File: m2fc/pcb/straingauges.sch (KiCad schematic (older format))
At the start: 81 parts, among them IC201 AD8226, IC202 AD8656, IC203 AD8541, IC204 AD8226, IC205 AD8656, IC206 AD8541, IC207 AD8226, IC208 AD8656, IC209 AD8541, K201 CONN_3, K202 CONN_3, K203 CONN_3, U201 HOUSING, U202 HOUSING, U203 HOUSING

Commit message: sd pullups, shielded sgs
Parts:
- removed K201, K202, K203: CONN_3, symbol CONN_3
- added P201, P202, P203: CONN_4, m2fc:S04B-PASK-2, symbol CONN_4
- C202: renamed from C209; footprint 0603 -> m2fc:C0603
- C204: renamed from C222; footprint 0603 -> m2fc:C0603
- C206: renamed from C235; footprint 0603 -> m2fc:C0603
- C208: renamed from C210; footprint 0603 -> m2fc:C0603
- C210: renamed from C223; footprint 0603 -> m2fc:C0603
- C212: renamed from C236; footprint 0603 -> m2fc:C0603
- C214: renamed from C211; footprint 0603 -> m2fc:C0603
- C216: renamed from C224; footprint 0603 -> m2fc:C0603
- C218: renamed from C237; footprint 0603 -> m2fc:C0603
- C219: renamed from C201; footprint 0603 -> m2fc:C0603
- C220: renamed from C214; footprint 0603 -> m2fc:C0603
- C221: renamed from C227; footprint 0603 -> m2fc:C0603
- C222: renamed from C207; footprint 0603 -> m2fc:C0603
- C223: renamed from C220; footprint 0603 -> m2fc:C0603
- C224: renamed from C233; footprint 0603 -> m2fc:C0603
- C225: renamed from C202; footprint 0603 -> m2fc:C0603
- C226: renamed from C215; footprint 0603 -> m2fc:C0603
- C227: renamed from C228; footprint 0603 -> m2fc:C0603
- C228: renamed from C212; footprint 0603 -> m2fc:C0603
- C229: renamed from C225; footprint 0603 -> m2fc:C0603
- C230: renamed from C238; footprint 0603 -> m2fc:C0603
- C234: renamed from C208; footprint 0603 -> m2fc:C0603
- C235: renamed from C221; footprint 0603 -> m2fc:C0603
- C236: renamed from C234; footprint 0603 -> m2fc:C0603
- C237: renamed from C203; footprint 0603 -> m2fc:C0603
- C238: renamed from C216; footprint 0603 -> m2fc:C0603
- C239: renamed from C229; footprint 0603 -> m2fc:C0603
- IC204: renamed from IC201; footprint SOIC8 -> m2fc:MSOP8
- IC205: renamed from IC204; footprint SOIC8 -> m2fc:MSOP8
- IC206: renamed from IC207; footprint SOIC8 -> m2fc:MSOP8
- IC207, IC208: renamed from IC202; footprint SOIC8 -> m2fc:SOIC8
- IC207, IC209: renamed from IC205; footprint SOIC8 -> m2fc:SOIC8
- IC208: footprint SOIC8 -> m2fc:SOIC8
- IC209: renamed from IC208; footprint SOIC8 -> m2fc:SOIC8
- R201, R211: footprint 0603 -> m2fc:R0603
- R202: renamed from R209; footprint 0603 -> m2fc:R0603
- R203: renamed from R217; footprint 0603 -> m2fc:R0603
- R204: renamed from R202; footprint 0603 -> m2fc:R0603
- R205: renamed from R208; footprint 0603 -> m2fc:R0603
- R206: renamed from R210; footprint 0603 -> m2fc:R0603
- R207: renamed from R216; footprint 0603 -> m2fc:R0603
- R208: renamed from R218; footprint 0603 -> m2fc:R0603
- R209: renamed from R224; footprint 0603 -> m2fc:R0603
- R210: renamed from R203; footprint 0603 -> m2fc:R0603
- R212: renamed from R219; footprint 0603 -> m2fc:R0603
- R213: renamed from R204; footprint 0603 -> m2fc:R0603
- R214: renamed from R212; footprint 0603 -> m2fc:R0603
- R215: renamed from R220; footprint 0603 -> m2fc:R0603
- R216: renamed from R205; footprint 0603 -> m2fc:R0603
- R217: renamed from R213; footprint 0603 -> m2fc:R0603
- R218: renamed from R221; footprint 0603 -> m2fc:R0603
- R219: renamed from R206; footprint 0603 -> m2fc:R0603
- R220: renamed from R214; footprint 0603 -> m2fc:R0603
- R221: renamed from R222; footprint 0603 -> m2fc:R0603
- R222: renamed from R207; footprint 0603 -> m2fc:R0603
- R223: renamed from R215; footprint 0603 -> m2fc:R0603
- R224: renamed from R223; footprint 0603 -> m2fc:R0603
- TP201, TP202, TP203: footprint (none) -> m2fc:TESTPAD
- U201, U202, U203: Farnell 1830728 -> 1830729
- renumbered C204 to C201, C217 to C203, C230 to C205, C205 to C207, C218 to C209, C231 to C211, C206 to C213, C219 to C215, C232 to C217, C213 to C231, C226 to C232, C239 to C233, IC203 to IC201, IC206 to IC202, IC209 to IC203
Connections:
- wire segments 225 -> 228

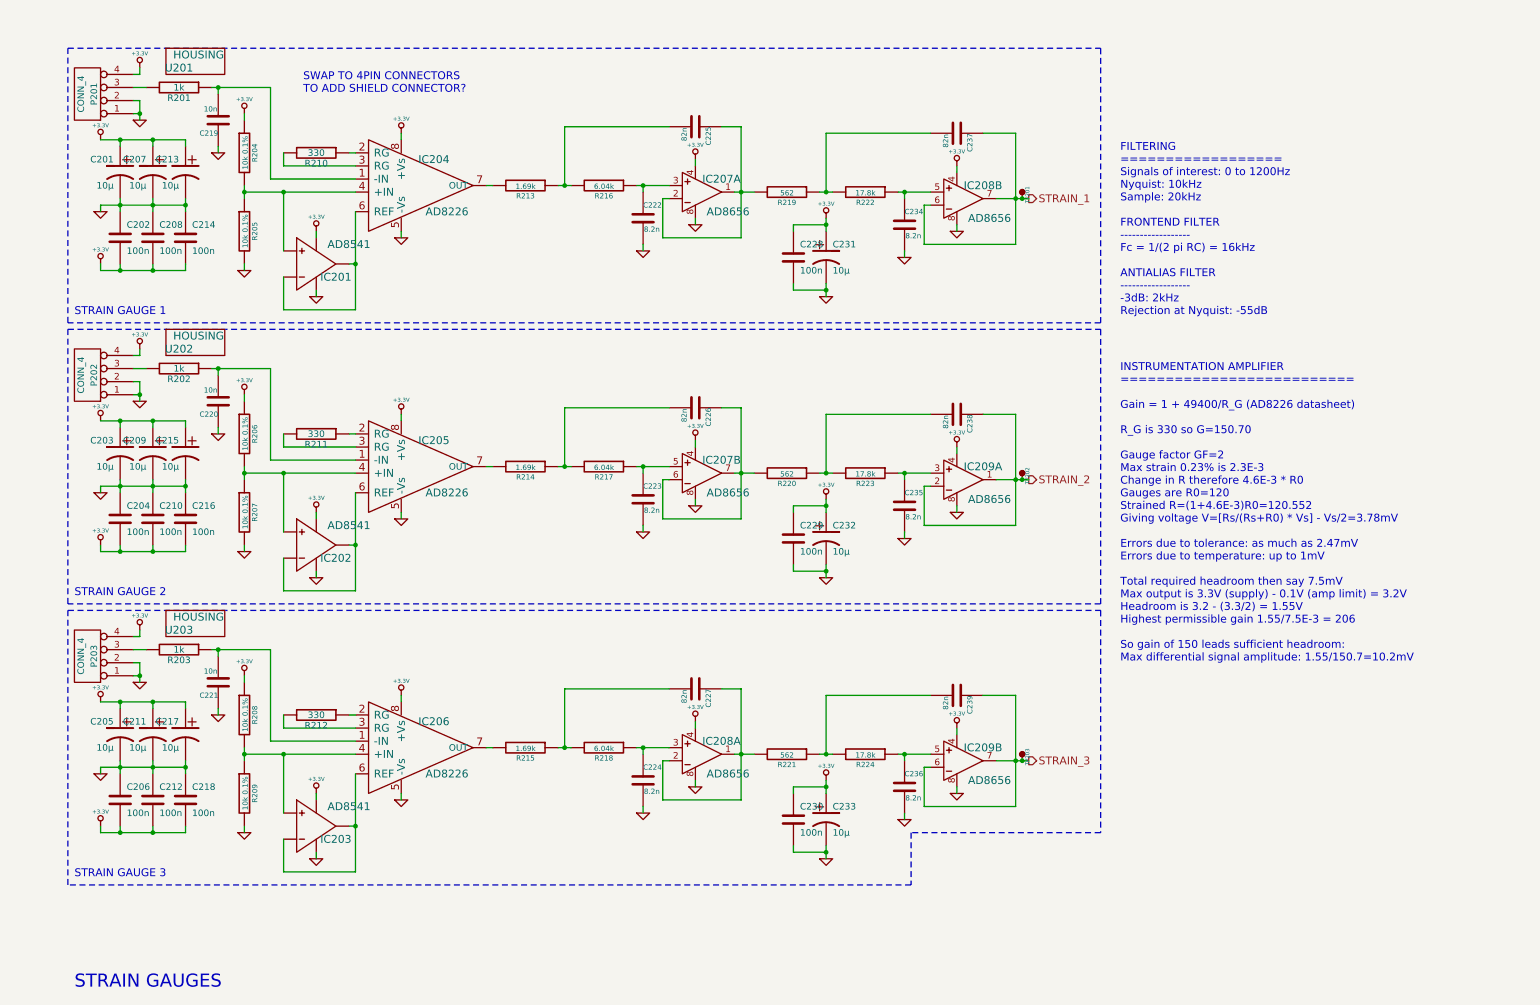
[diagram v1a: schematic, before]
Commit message: add esd diodes to m2fc
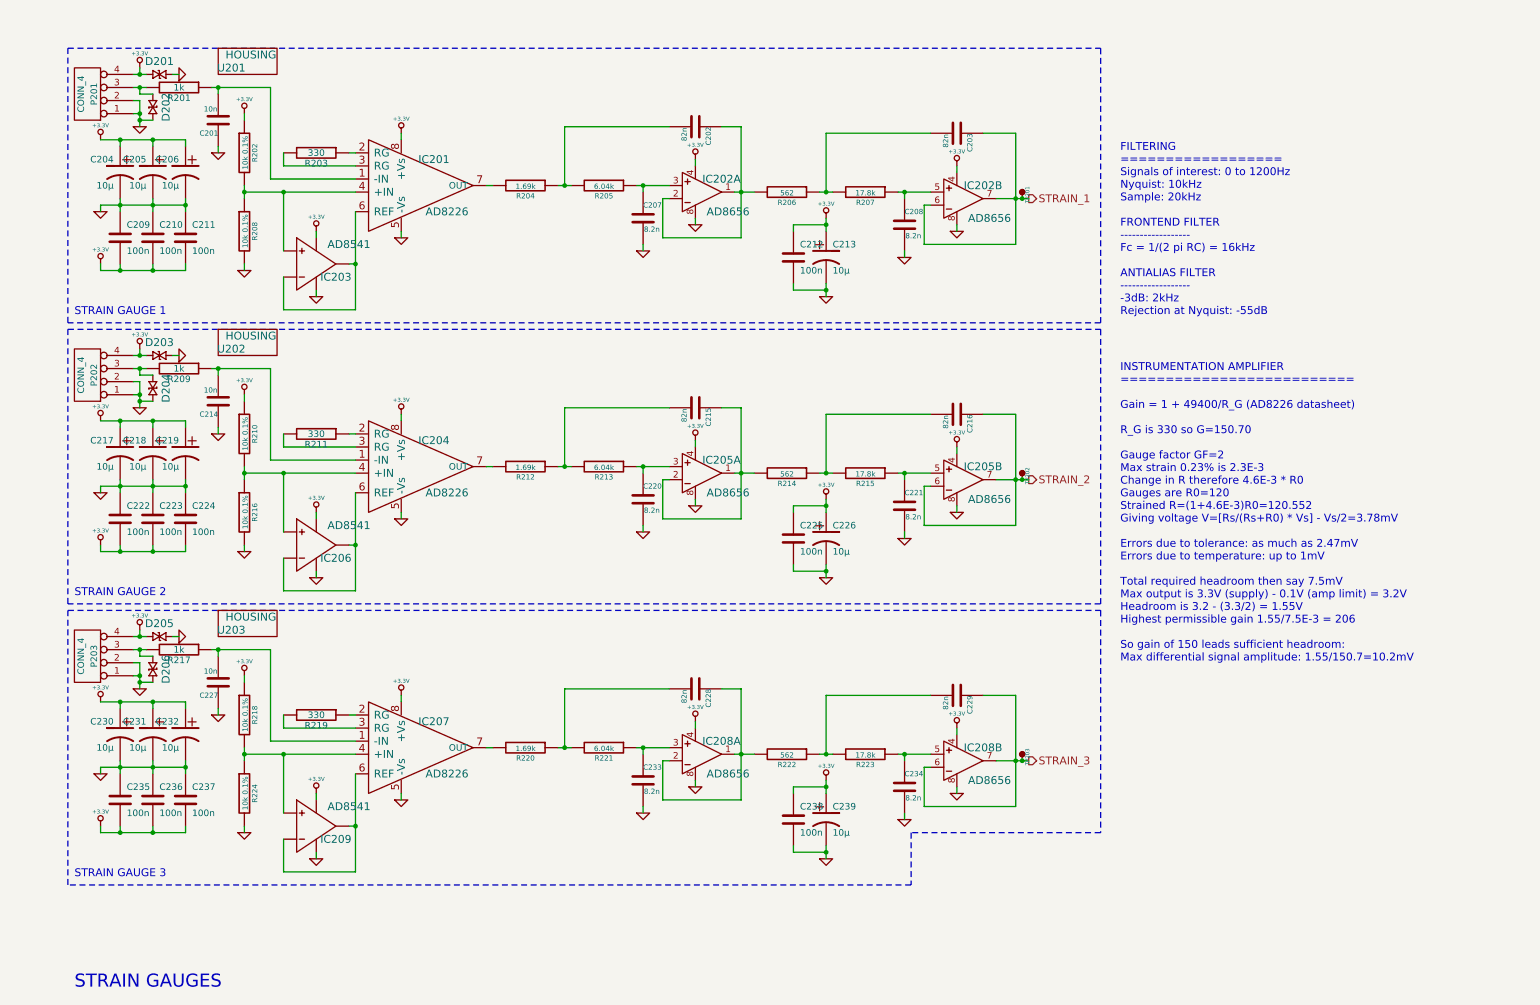
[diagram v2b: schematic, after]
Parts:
- added D201, D202, D203, D204, D205, D206: CGA0402MLC-12G, m2fc:R0402, symbol CGA0402MLC-12G
- C204: renamed from C201; footprint 1411 -> m2fc:C0603; Farnell 2333026 -> 1657936
- C205: renamed from C207; footprint 1411 -> m2fc:C0603; Farnell 2333026 -> 1657936
- C206: renamed from C213; footprint 1411 -> m2fc:C0603; Farnell 2333026 -> 1657936
- C213: renamed from C231; footprint 1411 -> m2fc:C0603; Farnell 2333026 -> 1657936
- C217: renamed from C203; footprint 1411 -> m2fc:C0603; Farnell 2333026 -> 1657936
- C218: renamed from C209; footprint 1411 -> m2fc:C0603; Farnell 2333026 -> 1657936
- C219: renamed from C215; footprint 1411 -> m2fc:C0603; Farnell 2333026 -> 1657936
- C226: renamed from C232; footprint 1411 -> m2fc:C0603; Farnell 2333026 -> 1657936
- C230: renamed from C205; footprint 1411 -> m2fc:C0603; Farnell 2333026 -> 1657936
- C231: renamed from C211; footprint 1411 -> m2fc:C0603; Farnell 2333026 -> 1657936
- C232: renamed from C217; footprint 1411 -> m2fc:C0603; Farnell 2333026 -> 1657936
- C239: renamed from C233; footprint 1411 -> m2fc:C0603; Farnell 2333026 -> 1657936
- renumbered C219 to C201, C225 to C202, C237 to C203, C222 to C207, C234 to C208, C202 to C209, C208 to C210, C214 to C211, C228 to C212, C220 to C214, C226 to C215, C238 to C216, C223 to C220, C235 to C221, C204 to C222, C210 to C223, C216 to C224, C229 to C225, C221 to C227, C227 to C228, C239 to C229, C224 to C233, C236 to C234, C206 to C235, C212 to C236, C218 to C237, C230 to C238, IC204 to IC201, IC207 to IC202, IC208 to IC202, IC201 to IC203, IC205 to IC204, IC207 to IC205, IC209 to IC205, IC202 to IC206, IC206 to IC207, IC209 to IC208, IC203 to IC209, R204 to R202, R210 to R203, R213 to R204, R216 to R205, R219 to R206, R222 to R207, R205 to R208, R202 to R209, R206 to R210, R214 to R212, R217 to R213, R220 to R214, R223 to R215, R207 to R216, R203 to R217, R208 to R218, R212 to R219, R215 to R220, R218 to R221, R221 to R222, R224 to R223, R209 to R224
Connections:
- net +3.3V: now also D201.2, D203.2, D205.2
- net GND: now also D201.1, D202.1, D203.1, D204.1, D205.1, D206.1
- net STRAIN_2: now also IC205.6 (-IN), IC205.7 (OUT); no longer IC205.1 (OUT), IC205.2 (-IN)
- net at P201.3 (P3), R201.2: now also D202.2
- net at P202.3 (P3), R209.2: now also D204.2
- net at C220.1, R213.1: now also IC205.3 (+IN); no longer IC205.5 (+IN)
- net at C215.1, R214.2: now also IC205.1 (OUT), IC205.2 (-IN); no longer IC205.6 (-IN), IC205.7 (OUT)
- net at C221.1, R215.1: now also IC205.5 (+IN); no longer IC205.3 (+IN)
- net at P203.3 (P3), R217.2: now also D206.2
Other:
- note removed: "SWAP TO 4PIN CONNECTORS\nTO ADD SHIELD CONNECTOR?"
- moved on the sheet: U201, U202, U203

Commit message: m2fc footprints, start layout
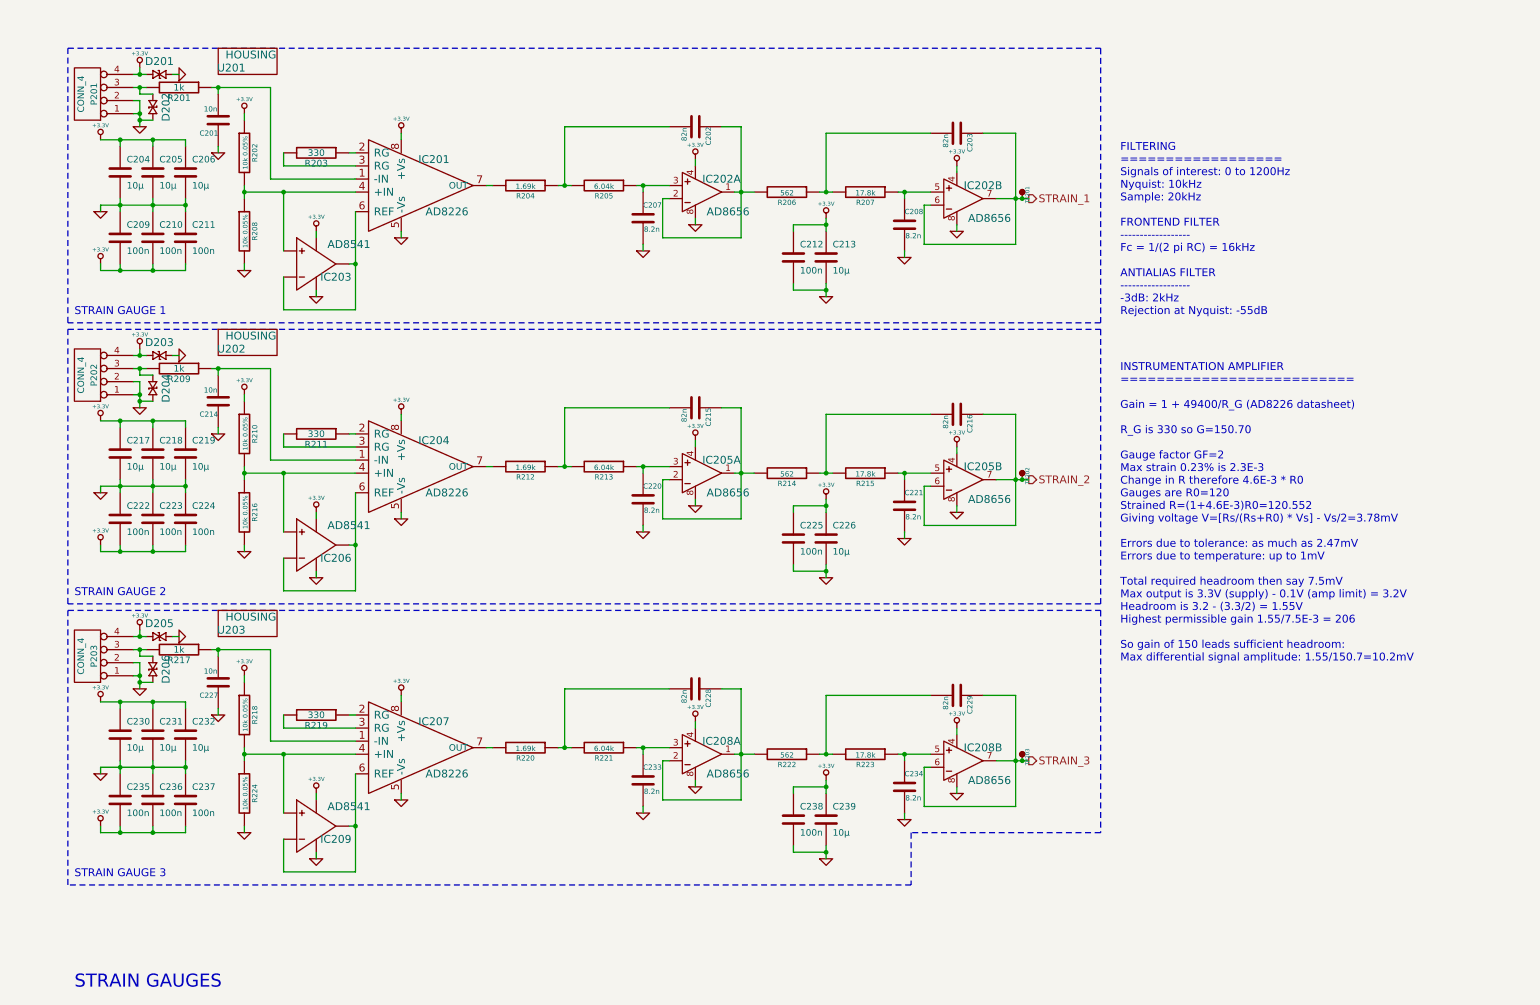
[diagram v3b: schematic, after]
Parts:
- removed C204, C205, C206, C213, C217, C218, C219, C226, C230, C231, C232, C239: 10µ, m2fc:C0603, symbol CP1
- added C204, C205, C206, C213, C217, C218, C219, C226, C230, C231, C232, C239: 10µ, m2fc:C0603, symbol C
- IC201, IC204, IC207: Farnell 1827360 -> 1827359
- IC202, IC205, IC208: footprint m2fc:SOIC8 -> m2fc:MSOP8; Farnell 1117887 -> 1858055
- IC203, IC206, IC209: footprint SC-70-5 -> m2fc:SC-70-5
- P201, P202, P203: Farnell (none) -> 1830749
- R202, R208, R210, R216, R218, R224: value 10k 0.1% -> 10k 0.05%
- R206, R214, R222: Farnell 2117134 -> 2116652
- R207, R215, R223: Farnell 2117295 -> 2116811
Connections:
- net +3.3V: now also C204.1, C205.1, C206.1, C213.1, C217.1, C218.1, C219.1, C226.1, C230.1, C231.1, C232.1, C239.1
- net GND: now also C204.2, C205.2, C206.2, C213.2, C217.2, C218.2, C219.2, C226.2, C230.2, C231.2, C232.2, C239.2

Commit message: paid off woo
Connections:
- net +3.3V renamed VAA
